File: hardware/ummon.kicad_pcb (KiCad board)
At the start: 4 copper layers, 60 x 60 mm, 95 parts, among them J1 Conn_01x08_Pin, J2 Conn_01x05_Pin, J3 Conn_01x04_Pin, J4 Conn_01x04_Pin, J5 Conn_01x04_Pin, P1 Display, Q1 SI1308EDL, SW1 Reboot, SW2 Flash, SW3 Test Button, SW4 MINI MSK12CO2, U1 ESP32-C6-WROOM-1-N8, U2 SCD41, U3 SGP41, U4 SHT41, U5 AMS1117-3.3

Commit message: :construction: WIP reverse display pinout and unplace epd section
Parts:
- moved Q1 53.5 mm to (115.2, 172.8)
- moved R10 51.4 mm to (98.8, 144.4)
- moved R11 51.4 mm to (111.5, 147.7)
- moved SW4 51.4 mm to (103.8, 146.6)
- moved R16 51.4 mm to (96.9, 144.4)
- moved R13 51.4 mm to (111.5, 145.8)
- moved R9 41.7 mm to (117.8, 154.8)
- moved C22 39.7 mm to (135.2, 163.1)
- moved C26 39.7 mm to (128.2, 168.2)
- moved D4 39.7 mm to (127.1, 164.4)
- moved TP5 39.7 mm to (113.3, 170.1)
- moved C25 39.7 mm to (115.0, 162.2)
- moved C32 39.7 mm to (116.3, 170.3)
- moved D3 39.7 mm to (125.3, 164.4)
- moved TP6 39.7 mm to (123.0, 162.4)
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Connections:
- P1 pad 1: unconnected-(P1-Pad1) -> Net-(C38-Pad2)
- P1 pad 10: /EPD_RST -> +3.3V
- P1 pad 11: /EPD_DC -> /EPD_DIN
- P1 pad 12: /EPD_CS -> /EPD_SCK
- P1 pad 13: /EPD_SCK -> /EPD_CS
- P1 pad 14: /EPD_DIN -> /EPD_DC
- P1 pad 15: +3.3V -> /EPD_RST
- P1 pad 16: +3.3V -> /EPD_BUSY
- P1 pad 17: GND -> /EPD_BS
- P1 pad 18: Net-(C28-Pad2) -> unconnected-(P1-Pad18)
- P1 pad 19: Net-(C29-Pad2) -> unconnected-(P1-Pad19)
- P1 pad 2: /EPD_GDR -> /EPD_PREVGL
- P1 pad 20: Net-(C30-Pad2) -> Net-(C24-Pad2)
- P1 pad 21: /EPD_PREVGH -> Net-(C23-Pad2)
- P1 pad 22: Net-(C34-Pad2) -> /EPD_RESE
- P1 pad 23: /EPD_PREVGL -> /EPD_GDR
- P1 pad 24: Net-(C38-Pad2) -> unconnected-(P1-Pad24)
- P1 pad 25: GND -> unconnected-(P1-Pad25)
- P1 pad 26: GND -> unconnected-(P1-Pad26)
- P1 pad 3: /EPD_RESE -> Net-(C34-Pad2)
- P1 pad 4: Net-(C23-Pad2) -> /EPD_PREVGH
- P1 pad 5: Net-(C24-Pad2) -> Net-(C30-Pad2)
- P1 pad 6: unconnected-(P1-Pad6) -> Net-(C29-Pad2)
- P1 pad 7: unconnected-(P1-Pad7) -> Net-(C28-Pad2)
- P1 pad 8: /EPD_BS -> GND
- P1 pad 9: /EPD_BUSY -> +3.3V
- U1 pad 16: /EPD_BUSY -> /EPD_DIN
- U1 pad 17: /EPD_RST -> /EPD_SCK
- U1 pad 18: /EPD_DC -> /EPD_CS
- U1 pad 19: /EPD_CS -> /EPD_DC
- U1 pad 20: /EPD_SCK -> /EPD_RST
- U1 pad 21: /EPD_DIN -> /EPD_BUSY
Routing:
- net /I2C_SCL: track 185.7 -> 129.7 mm
- net GND: track 164.6 -> 111.9 mm, vias 59 -> 34
- net /EPD_DC: track 49.1 -> 0.00 mm, vias 2 -> 0
- net /EPD_DIN: track 48.5 -> 0.00 mm, vias 2 -> 0
- net /EPD_RST: track 48.5 -> 0.00 mm, vias 2 -> 0
- net /EPD_SCK: track 47.9 -> 0.00 mm, vias 2 -> 0
- net /EPD_CS: track 47.7 -> 0.00 mm, vias 2 -> 0
- net /EPD_BUSY: track 47.3 -> 0.00 mm, vias 2 -> 0
- net /GPIO0: track 39.3 -> 0.00 mm, vias 2 -> 0
- net /EPD_GDR: track 37.7 -> 0.00 mm
- net /GPIO2: track 36.6 -> 0.00 mm, vias 2 -> 0
- net /EPD_RESE: track 36.4 -> 0.00 mm
- net +3.3V: track 122.7 -> 94.3 mm, vias 22 -> 19
- net /EPD_PREVGL: track 26.3 -> 0.00 mm, vias 2 -> 0
- net /EPD_PREVGH: track 24.3 -> 0.00 mm, vias 2 -> 0
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
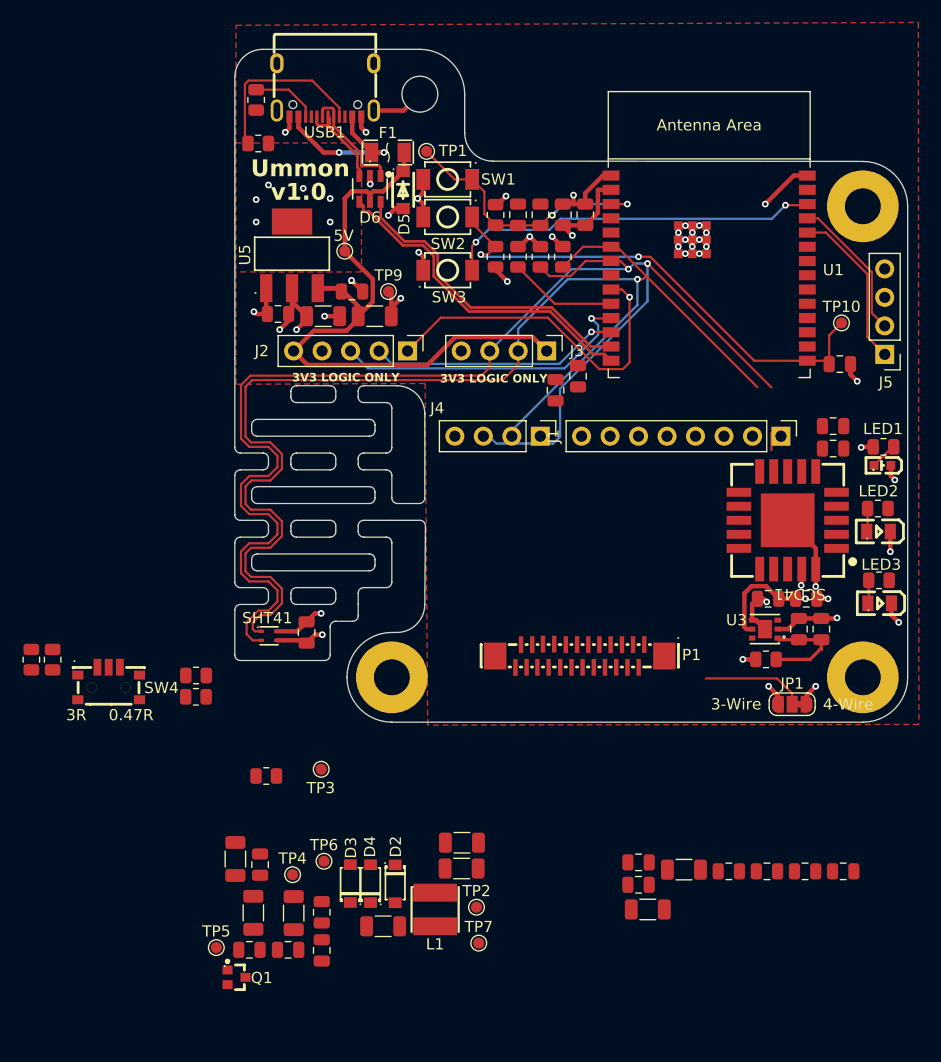
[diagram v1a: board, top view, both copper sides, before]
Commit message: :construction: WIP reposition epd section for flipped connector
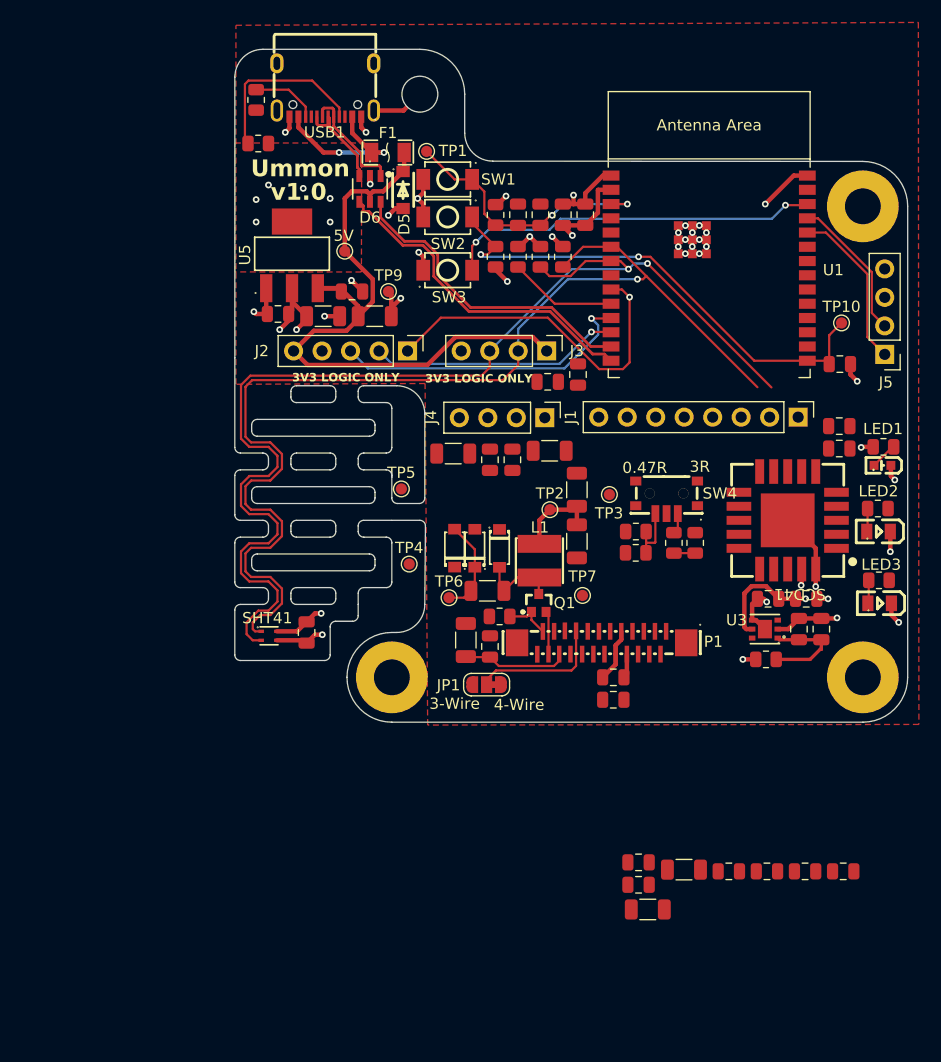
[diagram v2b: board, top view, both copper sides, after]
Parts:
- moved R16 60.1 mm to (156.1, 134.0), turned to -90 degrees
- moved R10 56.4 mm to (154.2, 134.0), turned to 90 degrees
- moved SW4 52.4 mm to (153.5, 129.9), turned to 180 degrees
- moved C32 48.7 mm to (137.8, 126.6), turned to 90 degrees
- moved C36 48.1 mm to (139.8, 126.6), turned to -90 degrees
- moved C37 47.1 mm to (143.1, 125.8), turned to 180 degrees
- moved C33 44.7 mm to (134.5, 126.0), turned to 180 degrees
- moved TP5 44.1 mm to (129.8, 129.2)
- moved Q1 42.9 mm to (142.1, 139.4), turned to -90 degrees
- moved R11 41.9 mm to (150.8, 133.0), turned to 0 degrees
- moved R13 40.7 mm to (150.8, 134.9), turned to 0 degrees
- moved TP2 36.1 mm to (143.1, 131.1)
- moved TP3 35.5 mm to (148.4, 129.7)
- moved C22 35.3 mm to (145.5, 129.3), turned to -90 degrees
- moved C39 34.3 mm to (148.8, 148.0), turned to 180 degrees
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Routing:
- net /I2C_SCL: track 129.7 -> 103.4 mm
- net /I2C_SDA: track 118.9 -> 100.8 mm
- net Net-(C24-Pad2): track 0.00 -> 9.46 mm
- net +3.3V: track 94.3 -> 103.3 mm, vias 19 -> 18
- net /EPD_VGL: track 0.00 -> 8.59 mm
- net /EPD_VGH: track 0.00 -> 7.41 mm
- net Net-(R11-Pad2): track 0.00 -> 5.30 mm
- net /EPD_GDR: track 0.00 -> 4.25 mm
- net /EPD_RESE: track 0.00 -> 3.85 mm
- net /EPD_BS: track 9.21 -> 12.0 mm
- net Net-(R10-Pad1): track 0.00 -> 1.90 mm
- net Net-(R10-Pad2): track 0.00 -> 1.84 mm
- net GND: track 111.9 -> 112.2 mm, vias 34 -> 33

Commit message: :sparkles: Completes routing after connector flip
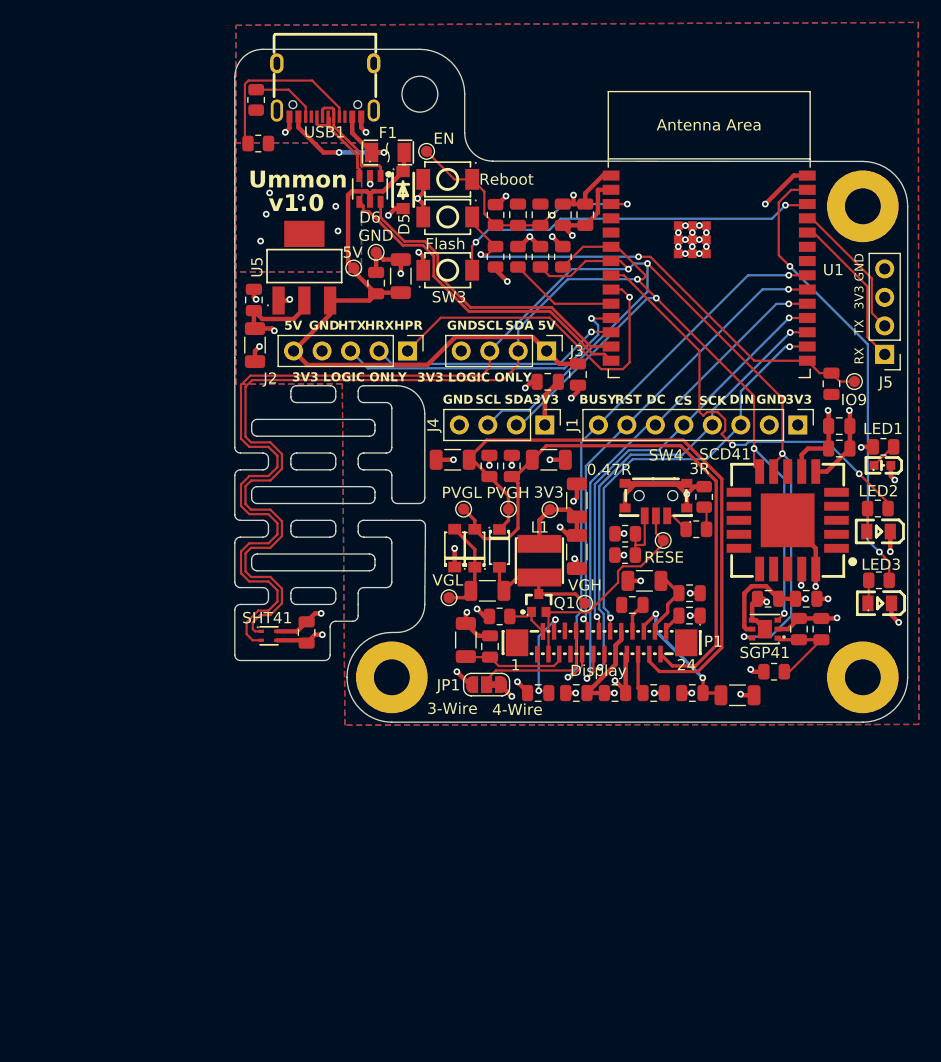
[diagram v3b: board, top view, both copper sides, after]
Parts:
- R4: value 3.3kΩ -> 10kΩ
- moved C23 31.5 mm to (142.1, 147.4), turned to 0 degrees
- moved C35 29.3 mm to (151.5, 137.4), turned to 0 degrees
- moved C28 28.3 mm to (150.4, 139.6)
- moved C34 26.4 mm to (155.6, 138.5)
- moved C38 22.5 mm to (155.6, 140.5), turned to 180 degrees
- moved C29 18.8 mm to (152.3, 147.4)
- moved C31 16.3 mm to (159.8, 147.6), turned to 180 degrees
- moved C30 16.2 mm to (155.8, 147.4), turned to 0 degrees
- moved TP4 10.1 mm to (139.4, 131.0)
- moved C37 8.69 mm to (134.4, 126.6), turned to 0 degrees
- moved C33 8.54 mm to (143.0, 126.6), turned to 0 degrees
- moved C17 6.60 mm to (116.8, 116.4), turned to -90 degrees
- moved TP3 6.31 mm to (153.2, 133.8)
- moved TP5 5.83 mm to (135.4, 131.0)
- moved TP10 5.35 mm to (170.2, 119.6)
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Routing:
- net /EPD_PREVGH: track 0.00 -> 56.4 mm
- net /EPD_PREVGL: track 0.00 -> 53.1 mm
- net /EPD_BUSY: track 0.00 -> 50.5 mm, vias 0 -> 2
- net /I2C_SCL: track 103.4 -> 153.9 mm, vias 2 -> 4
- net GND: track 112.2 -> 158.3 mm, vias 33 -> 57
- net /EPD_DC: track 0.00 -> 46.0 mm, vias 0 -> 2
- net /EPD_SCK: track 0.00 -> 42.8 mm, vias 0 -> 2
- net /I2C_SDA: track 100.8 -> 142.3 mm, vias 1 -> 4
- net /EPD_RST: track 0.00 -> 41.3 mm, vias 0 -> 2
- net /GPIO2: track 0.00 -> 40.8 mm, vias 0 -> 2
- net /GPIO0: track 0.00 -> 38.5 mm, vias 0 -> 2
- net /EPD_CS: track 0.00 -> 38.5 mm, vias 0 -> 2
- net /EPD_DIN: track 0.00 -> 38.2 mm, vias 0 -> 2
- net +3.3V: track 103.3 -> 124.1 mm, vias 18 -> 21
- net /EPD_RESE: track 3.85 -> 20.2 mm
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- added copper zone on B.Cu, net +3.3V
- added copper zone on B.Cu, net GND

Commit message: wip
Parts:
- removed C23, C29: 1μF/50V, Capacitor_SMD:C_0805_2012Metric
- removed C25, C31, C33, C35, C37: 4.7μF/50V, Capacitor_SMD:C_1206_3216Metric
- removed C39: 10μF/50V, Capacitor_SMD:C_0805_2012Metric
- removed J1: Conn_01x08_Pin, Connector_PinHeader_2.54mm:PinHeader_1x08_P2.54mm_Vertical
- removed JP1: BS_Jumper, Jumper:SolderJumper-3_P1.3mm_Bridged12_RoundedPad1.0x1.5mm_NumberLabels
- removed L1: 68μH, parts:IND-SMD_L4.0-W4.0_FNR40XXS
- added C19: 100nF, Capacitor_SMD:C_0805_2012Metric, F.Cu at (147.7, 155.9)
- added C21: 100nF, Capacitor_SMD:C_0805_2012Metric, F.Cu at (153.1, 163.9)
- added J6: Conn_01x09_Pin, Connector_PinHeader_2.54mm:PinHeader_1x09_P2.54mm_Vertical, F.Cu at (166.5, 123.5)
- added Q2: AO3401A, parts:SOT-23_L2.9-W1.3-P1.90-LS2.4-BR, F.Cu at (148.6, 170.3)
- added Q3: AO3401A, parts:SOT-23_L2.9-W1.3-P1.90-LS2.4-BR, F.Cu at (148.6, 174.5)
- added R17: 100kΩ, Resistor_SMD:R_0805_2012Metric, F.Cu at (148.7, 160.8)
- added R18: 4.7kΩ, Resistor_SMD:R_0805_2012Metric, F.Cu at (148.7, 163.7)
- added R19: 100kΩ, Resistor_SMD:R_0805_2012Metric, F.Cu at (148.7, 166.7)
- added U6: 10μH, parts:IND-SMD_L4.5-W4.0, F.Cu at (142.5, 134.8)
- C22: value 4.7μF/50V -> 4.7μF
- C24, C28, C30, C34, C36: value 1μF/50V -> 1μF/25V
- C27: value 1μF/50V -> 1μF/10V
- Q1: value SI1308EDL -> BSS138LT1G; footprint parts:SOT-323_L2.0-W1.3-P1.30-LS2.1-BR -> parts:SOT-23-3_L2.9-W1.6-P1.90-LS2.8-BR
- TP4: value PVGH -> PCP
- TP5: value PVGL -> PSW
- moved LED1 44.2 mm to (153.2, 166.7), turned to 0 degrees
- moved R14 42.4 mm to (143.3, 155.9)
- moved Q1 38.9 mm to (153.1, 176.7), turned to 0 degrees
- moved R1 2.22 mm to (165.3, 145.5)
- moved C4 1.47 mm to (170.1, 122.8)
- moved C5 1.47 mm to (170.1, 124.8)
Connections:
- net Net-(C24-Pad2) renamed /EPD_VSH2
- net Net-(C28-Pad2) renamed /EPD_VDD
- net Net-(C30-Pad2) renamed /EPD_VSH
- net Net-(C34-Pad2) renamed /EPD_VSL
- net Net-(C38-Pad2) renamed /EPD_VCOM
- C18 pad 2: +3.3V -> EPD_3V3
- C22 pad 2: +3.3V -> EPD_3V3
- C26 pad 1: /EPD_VGL -> /EPD_CP
- C26 pad 2: /EPD_VGH -> /EPD_SW
- C27 pad 2: +3.3V -> EPD_3V3
- C32 pad 1: /EPD_PREVGL -> GND
- C32 pad 2: GND -> /EPD_VGH
- C36 pad 2: /EPD_PREVGH -> /EPD_VGL
- D2 pad 1: /EPD_PREVGH -> /EPD_VGH
- D2 pad 2: /EPD_VGH -> /EPD_SW
- D3 pad 2: /EPD_VGL -> /EPD_CP
- D4 pad 1: /EPD_VGL -> /EPD_CP
- D4 pad 2: /EPD_PREVGL -> /EPD_VGL
- P1 pad 10: +3.3V -> EPD_3V3
- P1 pad 17: /EPD_BS -> GND
- P1 pad 2: /EPD_PREVGL -> /EPD_VGL
- P1 pad 21: Net-(C23-Pad2) -> unconnected-(P1-Pad21)
- P1 pad 25: unconnected-(P1-Pad25) -> GND
- P1 pad 26: unconnected-(P1-Pad26) -> GND
- P1 pad 4: /EPD_PREVGH -> /EPD_VGH
- P1 pad 6: Net-(C29-Pad2) -> unconnected-(P1-Pad6)
- P1 pad 9: +3.3V -> EPD_3V3
- Q1 pad 3: /EPD_VGH -> /EPD_SW
- R14 pad 1: +3.3V -> Net-(Q3-D)
- TP4 pad 1: /EPD_PREVGH -> /EPD_CP
- TP5 pad 1: /EPD_PREVGL -> /EPD_SW
- U1 pad 23: unconnected-(U1-IO15-Pad23) -> /EPD_PWR
- U1 pad 5: unconnected-(U1-IO5-Pad5) -> /GPIO5
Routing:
- net /EPD_PREVGH: track 56.4 -> 0.00 mm
- net /EPD_PREVGL: track 53.1 -> 0.00 mm
- net GND: track 158.3 -> 121.8 mm, vias 57 -> 37
- net +3.3V: track 124.1 -> 94.8 mm, vias 21 -> 16
- net /EPD_RESE: track 20.2 -> 0.00 mm
- net /EPD_VSH: track 12.5 -> 0.00 mm, vias 2 -> 0
- net /EPD_BS: track 12.0 -> 0.00 mm
- net /EPD_VGH: track 11.9 -> 0.00 mm
- net /EPD_VSH2: track 9.46 -> 0.00 mm
- net Net-(C23-Pad2): track 9.03 -> 0.00 mm, vias 2 -> 0
- net /EPD_VGL: track 8.59 -> 0.00 mm
- net /EPD_VSL: track 6.34 -> 0.00 mm
- net /EPD_GDR: track 4.25 -> 0.00 mm
- net Net-(C29-Pad2): track 3.65 -> 0.00 mm
- net /EPD_VDD: track 2.74 -> 0.00 mm
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
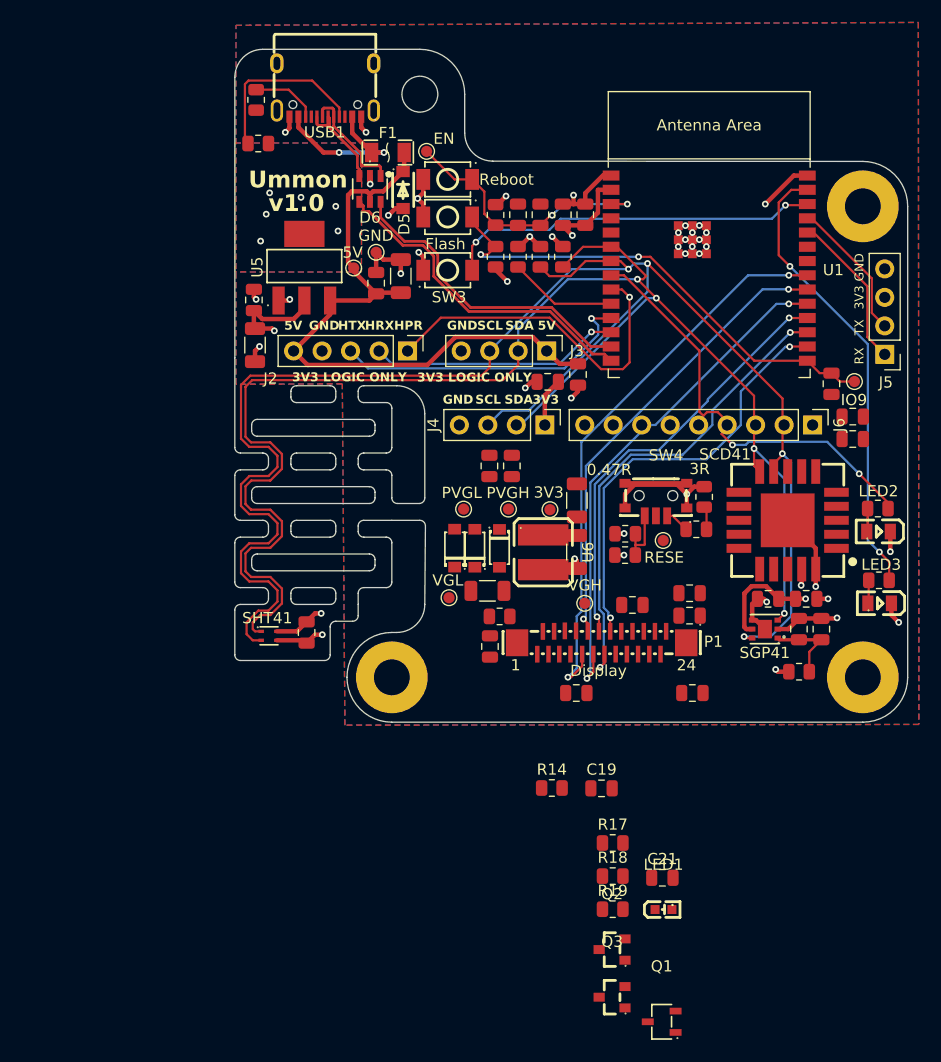
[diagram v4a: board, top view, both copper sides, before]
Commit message: :sparkles: Completes routing for epd rev 2.3
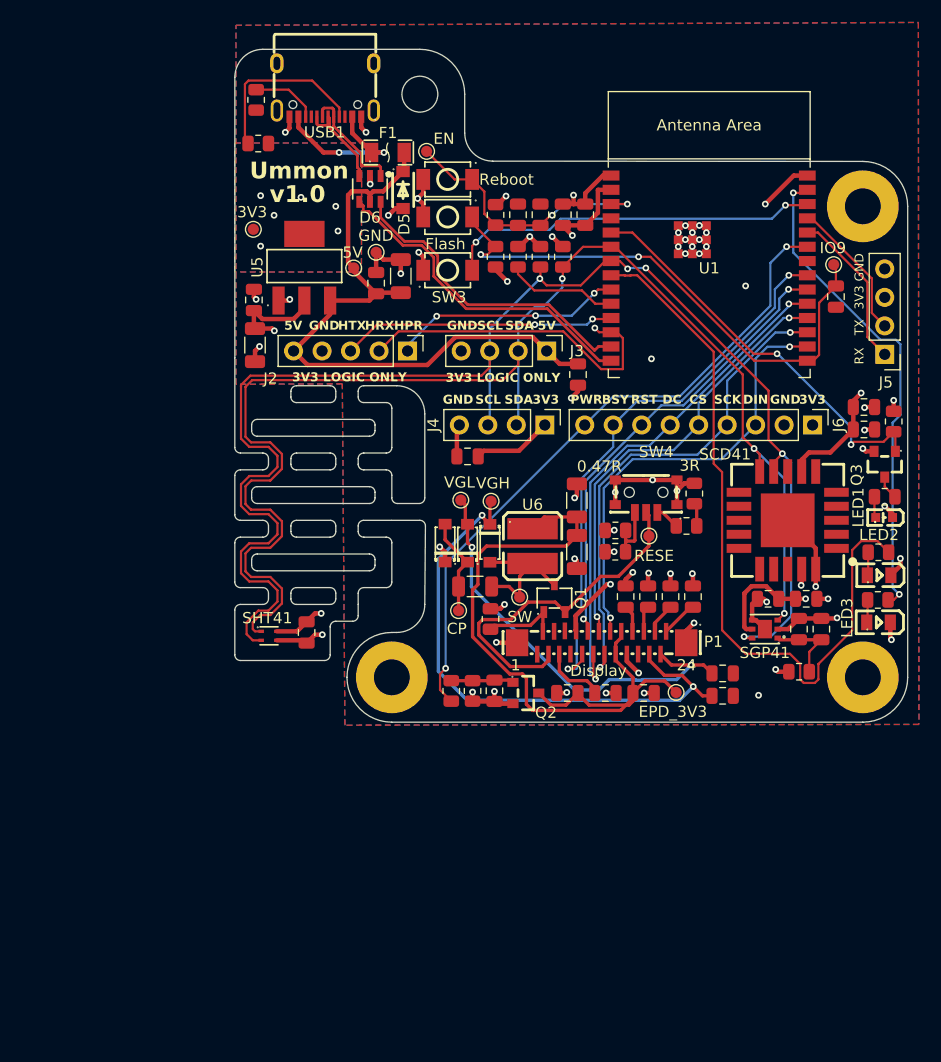
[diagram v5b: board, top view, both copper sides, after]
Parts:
- added TP11: EPD_3V3, TestPoint:TestPoint_Pad_D1.0mm, F.Cu at (154.3, 147.3)
- moved Q3 53.4 mm to (172.9, 127.0), turned to 90 degrees
- moved R19 50.2 mm to (173.8, 123.2), turned to 90 degrees
- moved LED1 40.1 mm to (172.9, 131.8), turned to 180 degrees
- moved R14 39.4 mm to (172.9, 129.9), turned to 180 degrees
- moved Q1 39.0 mm to (143.5, 138.9), turned to -90 degrees
- moved TP2 36.4 mm to (116.7, 106.0)
- moved C36 27.8 mm to (158.5, 145.7), turned to 180 degrees
- moved C32 27.8 mm to (158.5, 147.7), turned to 180 degrees
- moved Q2 24.1 mm to (140.9, 147.4), turned to 180 degrees
- moved R18 21.9 mm to (134.3, 147.2), turned to -90 degrees
- moved C21 18.5 mm to (144.7, 147.4), turned to 180 degrees
- moved R17 18.4 mm to (136.2, 147.2), turned to 90 degrees
- moved C19 12.9 mm to (138.2, 147.2), turned to 90 degrees
- moved TP7 12.4 mm to (137.8, 130.3)
- moved C24 11.1 mm to (148.1, 147.4), turned to 180 degrees
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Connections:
- net Net-(R10-Pad2) renamed /EPD_RESE_3O
- net Net-(R11-Pad2) renamed /EPD_RESE_0.47O
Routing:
- net EPD_3V3: track 0.00 -> 64.1 mm
- net /EPD_PWR: track 0.00 -> 59.1 mm, vias 0 -> 2
- net /EPD_VGH: track 0.00 -> 50.5 mm, vias 0 -> 2
- net /EPD_VGL: track 0.00 -> 37.8 mm, vias 0 -> 2
- net /GPIO5: track 0.00 -> 36.2 mm, vias 0 -> 2
- net /EPD_RESE: track 0.00 -> 31.1 mm
- net /GPIO0: track 38.5 -> 65.4 mm, vias 2 -> 0
- net GND: track 121.8 -> 146.5 mm, vias 37 -> 59
- net /I2C_SCL: track 153.9 -> 132.4 mm, vias 4 -> 5
- net +3.3V: track 94.8 -> 114.4 mm, vias 16 -> 20
- net /I2C_SDA: track 142.3 -> 126.4 mm, vias 4 -> 3
- net /EPD_SW: track 0.00 -> 12.9 mm
- net /H_PRESENCE: track 30.9 -> 20.7 mm, vias 1 -> 3
- net /EPD_CP: track 0.00 -> 8.87 mm
- net /EPD_GDR: track 0.00 -> 7.15 mm
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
